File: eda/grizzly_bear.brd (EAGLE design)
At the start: 76.2 x 41.3 mm, 65 parts, among them Q1 PSMN4R0, Q2 PSMN4R0, Q3 PSMN4R0, Q4 PSMN4R0, Q5 IPD90P03P4L, U1 A4940, U2 ATMEGA32U4-AU, U3 ACS714, U4 UA78L00, U5 ISL83491SOIC, Y1 16MHz

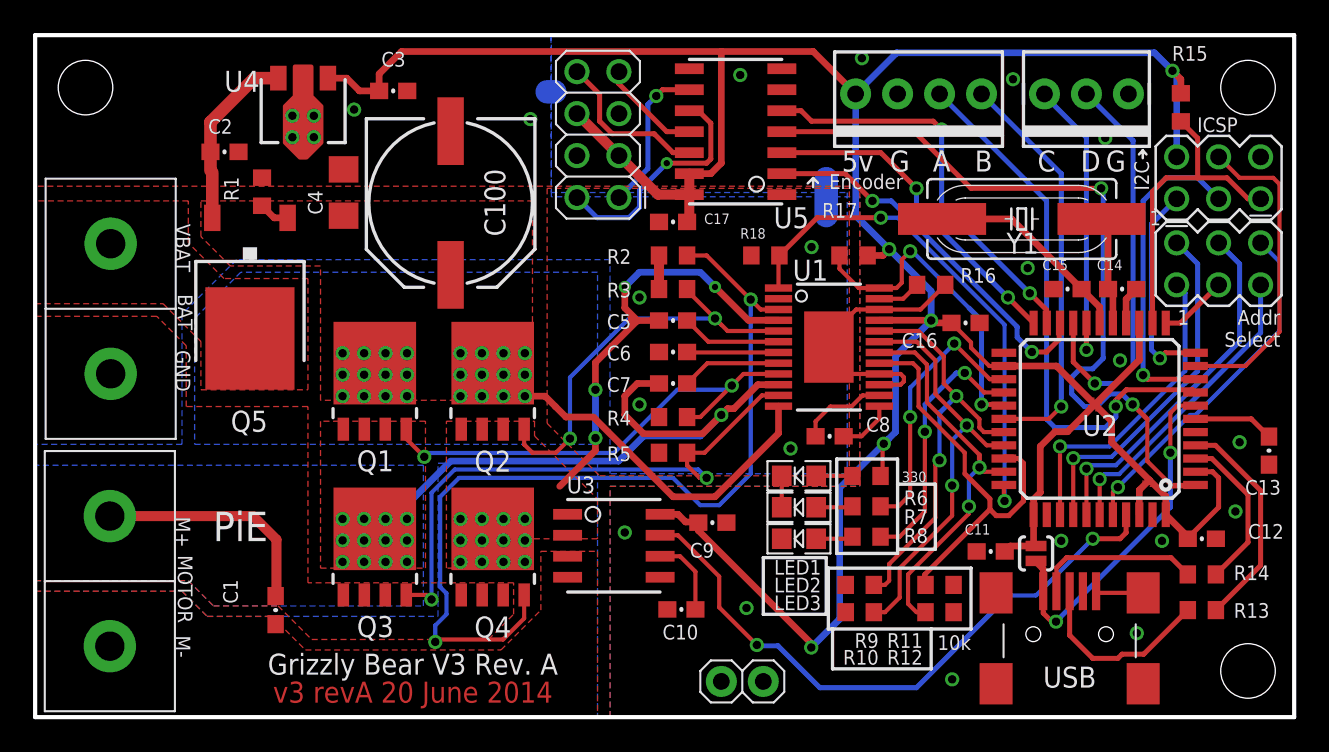
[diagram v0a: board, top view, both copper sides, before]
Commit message: Added test vias to Grizzly board
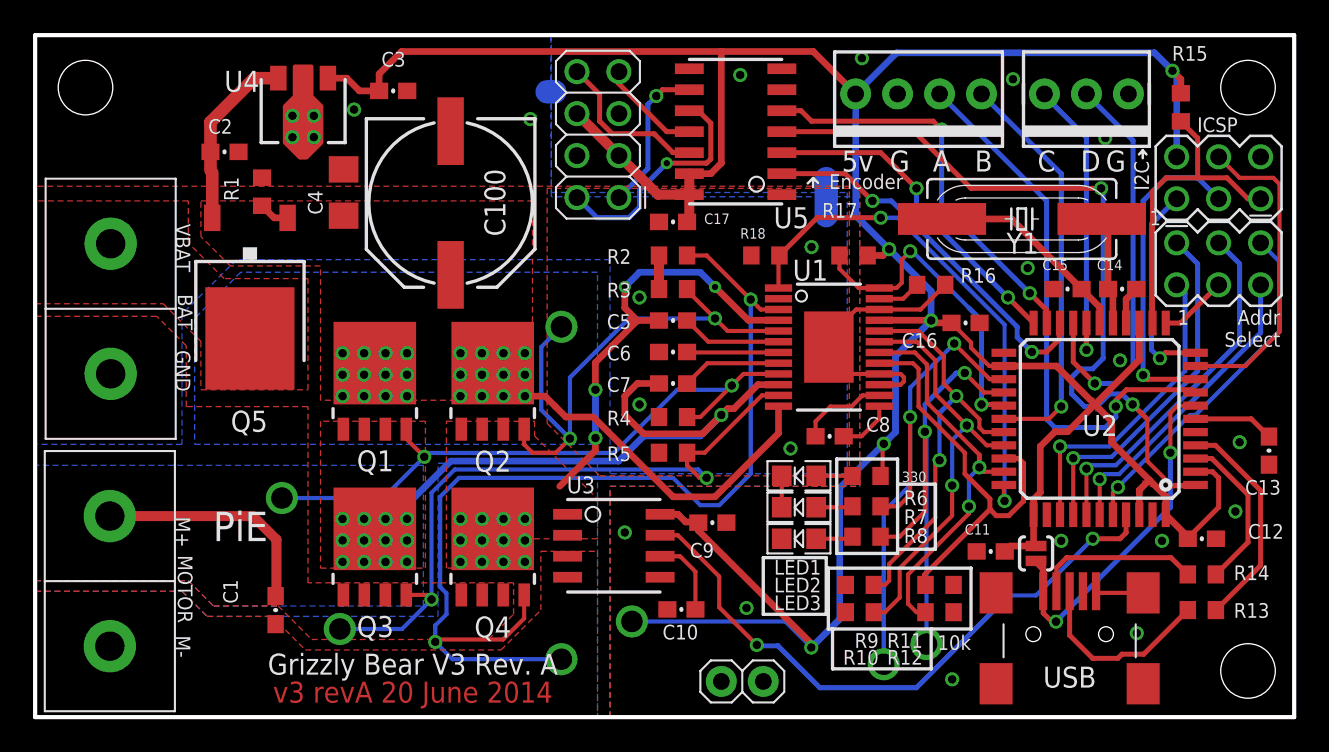
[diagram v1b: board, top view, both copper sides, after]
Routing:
- net RED: track 16.3 -> 31.9 mm, vias 2 -> 3
- net GREEN: track 16.1 -> 29.0 mm, vias 2 -> 3
- net 5V: track 192.5 -> 204.0 mm, vias 5 -> 6
- net GHA: track 29.1 -> 38.8 mm, vias 2 -> 3
- net GLB: track 54.8 -> 62.9 mm, vias 2 -> 3
- net GHB: track 24.9 -> 32.9 mm, vias 2 -> 3
- net GLA: track 34.8 -> 41.1 mm, vias 2 -> 3
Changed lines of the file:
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@@
 <wire x1="41.91" y1="19.812" x2="38.862" y2="19.812" width="0.254" layer="16"/>
 <contactref element="Q1" pad="4"/>
+<via x="14.9352" y="13.2588" extent="1-16" drill="1.3"/>
+<wire x1="14.9352" y1="13.2588" x2="21.0588" y2="13.2588" width="0.254" layer="16"/>
+<wire x1="21.0588" y1="13.2588" x2="23.553" y2="15.753" width="0.254" layer="16"/>
 </signal>
 <signal name="VBAT">
@@
 <wire x1="40.22" y1="14.478" x2="39.458" y2="15.24" width="0.254" layer="1"/>
 <contactref element="Q3" pad="4"/>
+<via x="18.4404" y="5.334" extent="1-16" drill="1.3"/>
+<wire x1="18.4404" y1="5.334" x2="22.204" y2="5.334" width="0.254" layer="16"/>
+<wire x1="22.204" y1="5.334" x2="23.99" y2="7.12" width="0.254" layer="16"/>
 </signal>
 <signal name="GLB">
@@
 <wire x1="40.64" y1="27.94" x2="43.307" y2="25.273" width="0.254" layer="1"/>
 <wire x1="43.307" y1="25.273" x2="43.91" y2="24.67" width="0.254" layer="1"/>
+<via x="31.8516" y="3.5052" extent="1-16" drill="1.3"/>
+<wire x1="25.2613" y1="3.5052" x2="24.2165" y2="4.55" width="0.254" layer="16"/>
+<wire x1="25.2613" y1="3.5052" x2="31.8516" y2="3.5052" width="0.254" layer="16"/>
 </signal>
 <signal name="GHB">
@@
 <wire x1="32.369" y1="16.855" x2="32.369" y2="20.558" width="0.254" layer="16"/>
 <wire x1="31.516" y1="16.002" x2="32.369" y2="16.855" width="0.254" layer="1"/>
-<wire x1="41.908" y1="23.37" x2="41.529" y2="23.749" width="0.254" layer="1"/>
 <contactref element="Q2" pad="4"/>
-<wire x1="41.529" y1="23.749" x2="41.148" y2="24.13" width="0.254" layer="1"/>
+<wire x1="41.908" y1="23.37" x2="41.148" y2="24.13" width="0.254" layer="1"/>
 <wire x1="39.458" y1="25.908" x2="39.458" y2="25.82" width="0.254" layer="1"/>
 <wire x1="39.458" y1="25.82" x2="41.148" y2="24.13" width="0.254" layer="1"/>
+<via x="31.8516" y="23.622" extent="1-16" drill="1.3"/>
+<wire x1="31.8516" y1="23.622" x2="30.6324" y2="22.4028" width="0.254" layer="16"/>
+<wire x1="30.6324" y1="22.4028" x2="30.6324" y2="18.5916" width="0.254" layer="16"/>
+<wire x1="30.6324" y1="18.5916" x2="32.369" y2="16.855" width="0.254" layer="16"/>
 </signal>
 <signal name="CB">
@@
 <wire x1="40.894" y1="32.893" x2="39.5926" y2="32.893" width="0.4064" layer="1"/>
 <wire x1="35.3314" y1="33.9852" x2="32.7914" y2="36.5252" width="0.6096" layer="1"/>
+<via x="36.1188" y="5.7912" extent="1-16" drill="1.3"/>
+<wire x1="36.1188" y1="5.7912" x2="45.3948" y2="5.7912" width="0.254" layer="16"/>
+<wire x1="45.3948" y1="5.7912" x2="46.972" y2="4.214" width="0.254" layer="16"/>
 </signal>
 <signal name="CP2">
@@
 <wire x1="53.848" y1="18.923" x2="55.753" y2="20.828" width="0.3048" layer="16"/>
 <wire x1="55.753" y1="20.828" x2="56.261" y2="20.828" width="0.3048" layer="16"/>
+<via x="53.9496" y="4.4196" extent="1-16" drill="1.3"/>
+<wire x1="53.9496" y1="4.4196" x2="53.9496" y2="17.1704" width="0.254" layer="16"/>
+<wire x1="53.9496" y1="17.1704" x2="53.848" y2="17.272" width="0.254" layer="16"/>
 </signal>
 <signal name="RED">
@@
 <wire x1="55.626" y1="22.606" x2="57.782" y2="20.45" width="0.254" layer="1"/>
 <wire x1="57.782" y1="20.45" x2="58.62800625" y2="20.45" width="0.254" layer="1"/>
+<via x="51.3588" y="3.2004" extent="1-16" drill="1.3"/>
+<wire x1="51.3588" y1="3.2004" x2="51.3588" y2="12.4206" width="0.254" layer="16"/>
+<wire x1="51.3588" y1="12.4206" x2="52.959" y2="14.0208" width="0.254" layer="16"/>
+<wire x1="52.959" y1="14.0208" x2="52.959" y2="18.161" width="0.254" layer="16"/>
 </signal>
 <signal name="RPP-GATE">

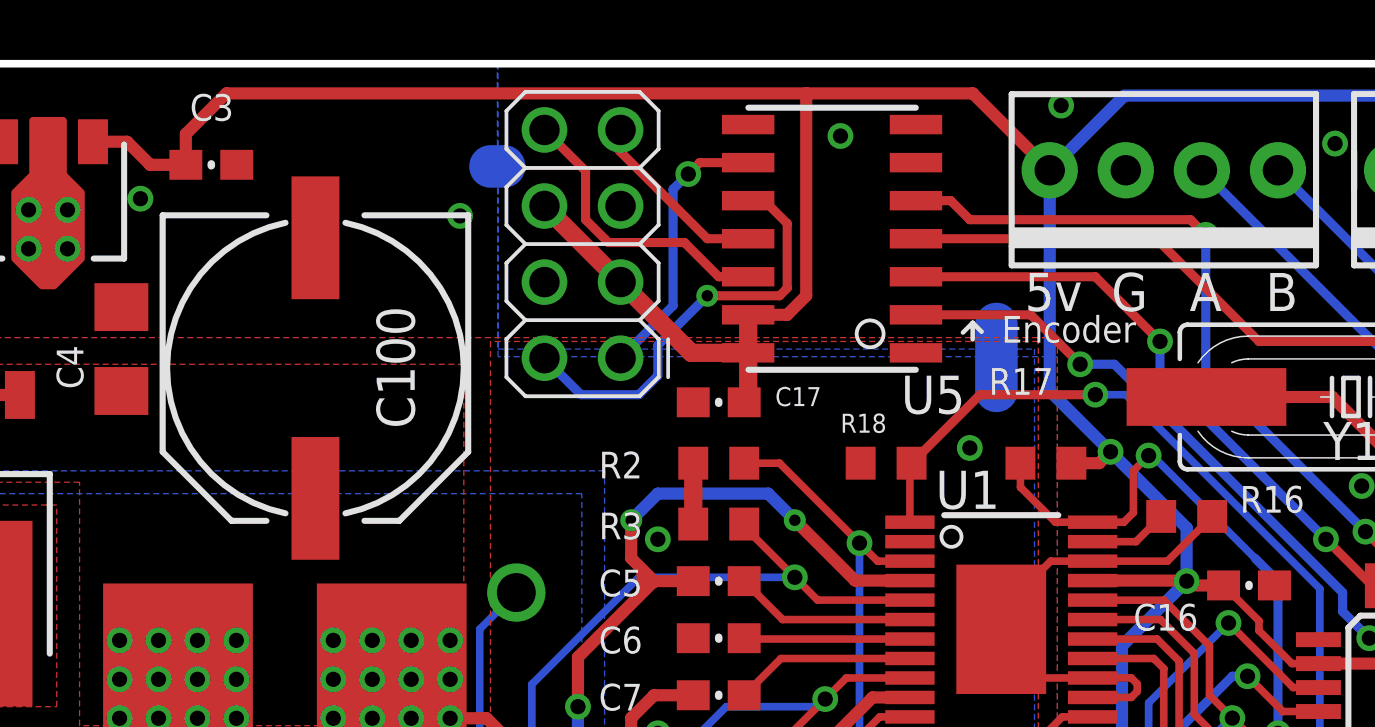
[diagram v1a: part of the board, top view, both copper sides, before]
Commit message: Change smartsensor connector to 2x5 on grizzly bear
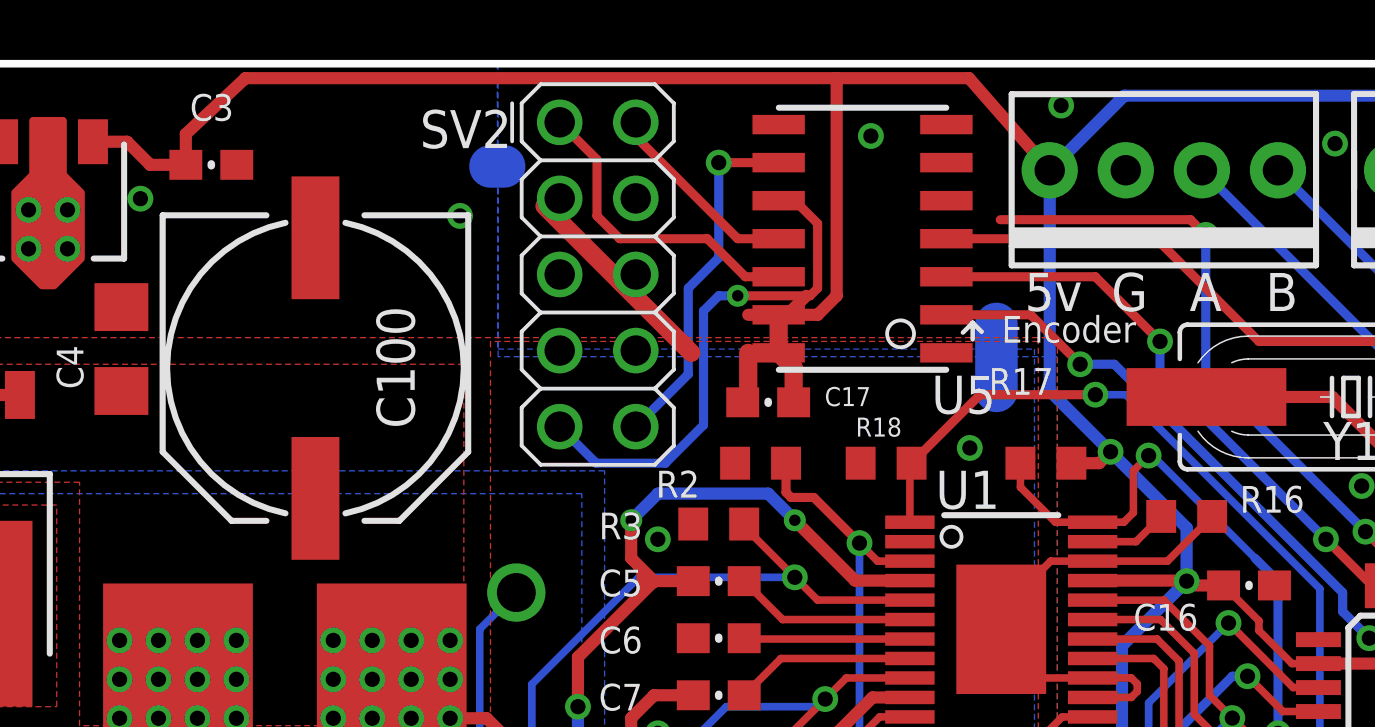
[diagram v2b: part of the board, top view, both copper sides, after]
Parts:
- SV2: value SENSOR_CONPTH -> (none); device pie:2X4 -> pie:2X5
- moved C17 1.65 mm to (40.3, 30.0)
- moved R2 1.40 mm to (40.0, 27.9)
- moved SV2 1.14 mm to (34.6, 34.2), turned to 270 degrees
- moved U5 1.02 mm to (43.4, 35.4)
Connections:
- new net SS_5V: SV2.5, SV2.6
- net A+: now also SV2.1; no longer SV2.8
- net A-: now also SV2.2; no longer SV2.7
- net B+: now also SV2.10; no longer SV2.1
- net B-: now also SV2.9; no longer SV2.2
- net GND: now also SV2.3, SV2.7, SV2.8; no longer SV2.5
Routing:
- net B-: track 14.5 -> 17.5 mm
- net TXD1: track 24.5 -> 21.4 mm
- net B+: track 9.24 -> 12.0 mm
- net GND: track 35.0 -> 33.0 mm
- net 5V: track 204.0 -> 206.0 mm
- net DE: track 47.9 -> 46.9 mm
- net RXD1: track 23.0 -> 21.9 mm
- net RE: track 20.1 -> 19.1 mm
- net GLB: track 62.9 -> 62.0 mm
- net A+: track 9.78 -> 10.5 mm

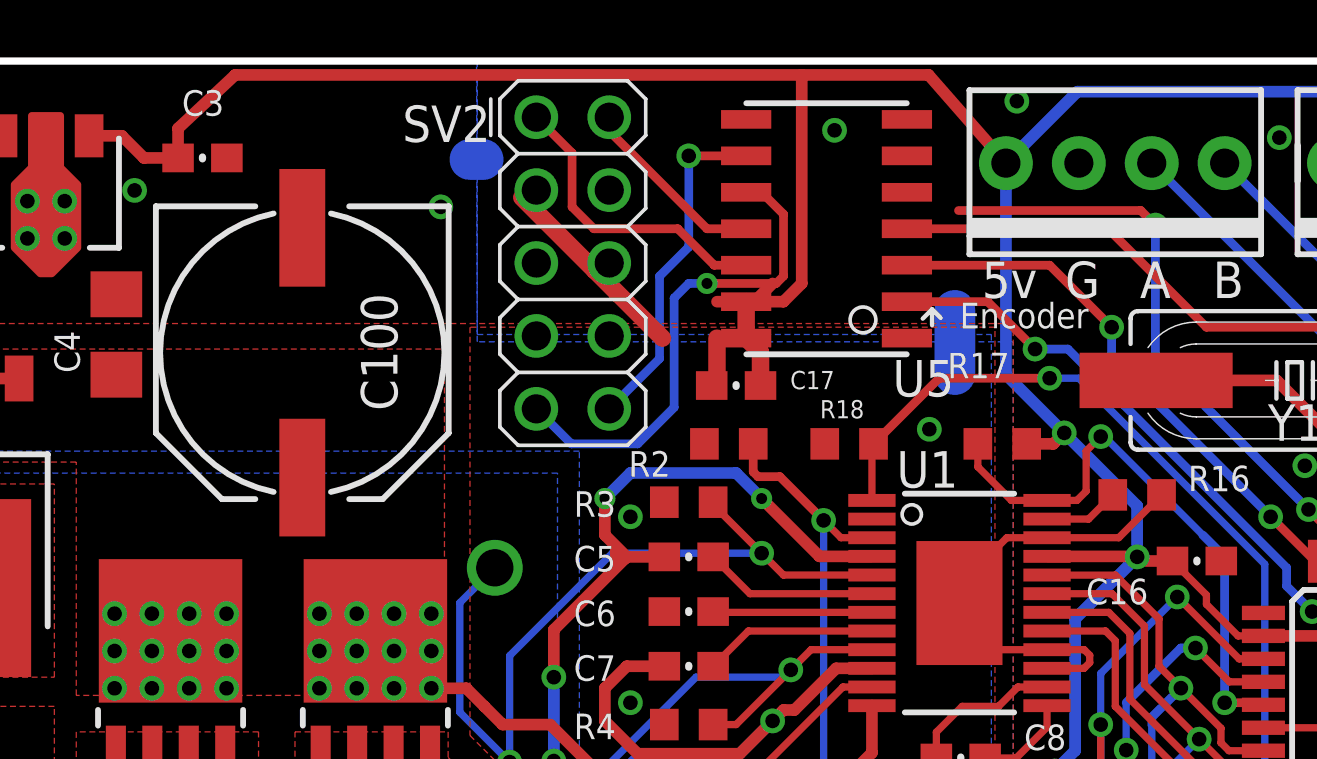
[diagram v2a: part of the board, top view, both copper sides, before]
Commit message: Minor routing fixes on grizzly and controller.
Edit rqou: Hopefully fixed fun merge problems between this commit
and Andrew Wang's.
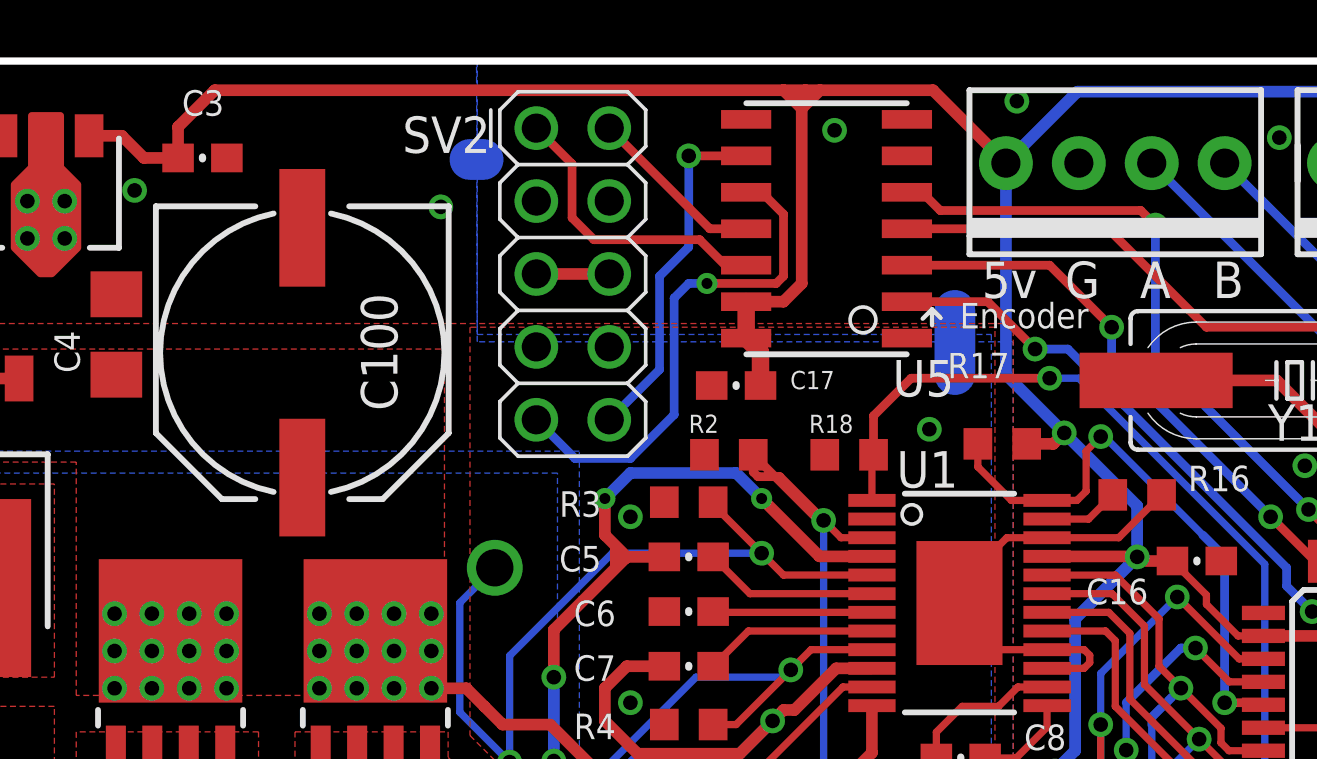
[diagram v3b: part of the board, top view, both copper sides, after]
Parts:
- moved R18 0.38 mm to (44.2, 27.6)
- moved R2 0.38 mm to (40.0, 27.6)
- moved SV2 0.38 mm to (34.6, 33.9)
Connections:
- net 5V: no longer SV2.3, SV2.6
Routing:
- net 5V: track 206.0 -> 196.0 mm
- net GLB: track 62.0 -> 65.4 mm
- net SS_5V: track 0.00 -> 2.54 mm
- net TXD1: track 21.4 -> 23.5 mm
- net DRIVER-RESET: track 30.9 -> 32.2 mm
